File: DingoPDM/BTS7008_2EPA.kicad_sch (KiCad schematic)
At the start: 13 parts, among them U11 BTS7008-2EPA

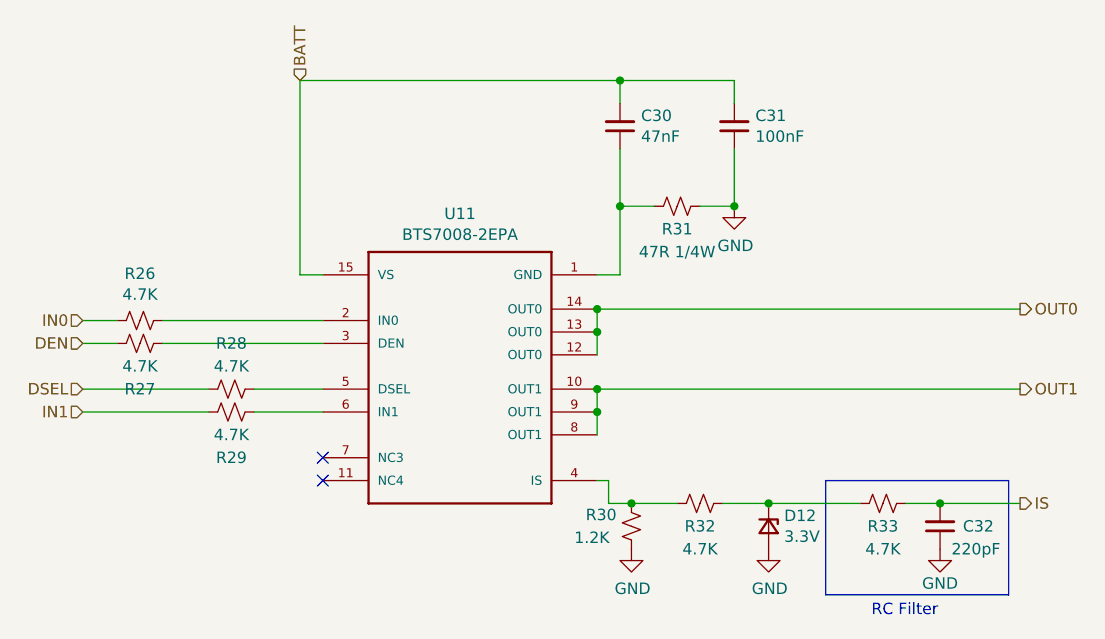
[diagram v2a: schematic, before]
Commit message: update to kicad 9.0.1
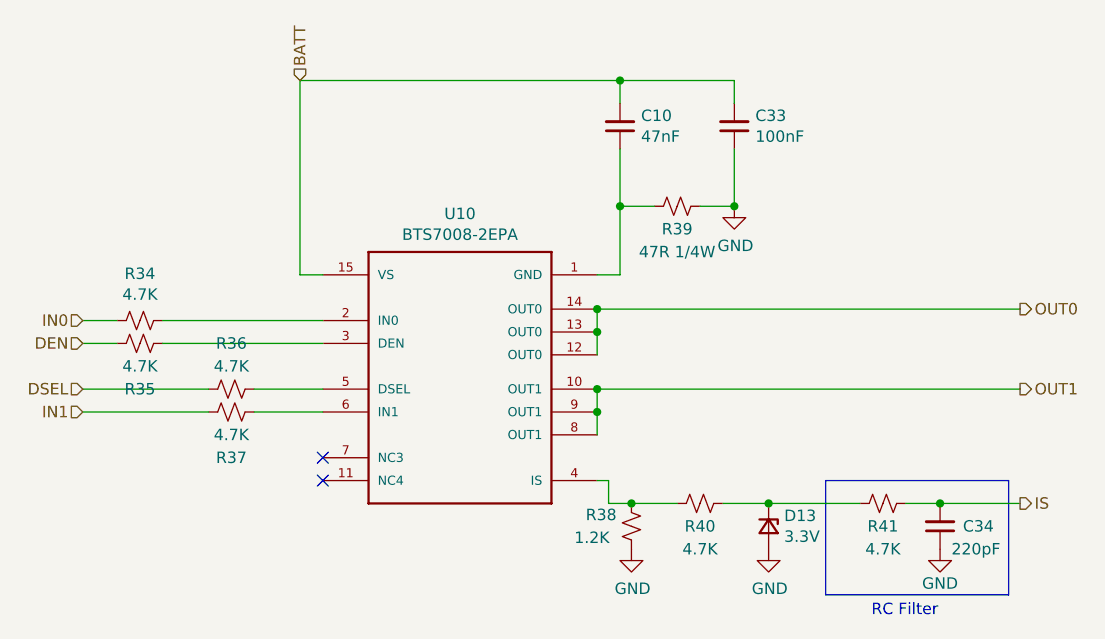
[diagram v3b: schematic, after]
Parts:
- renumbered C30 to C10, C31 to C33, C32 to C34, D12 to D13, R26 to R34, R27 to R35, R28 to R36, R29 to R37, R30 to R38, R31 to R39, R32 to R40, R33 to R41, U11 to U10
